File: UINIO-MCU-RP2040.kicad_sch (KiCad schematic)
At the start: 0 parts

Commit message: Part of the schematic diagram is drawn.
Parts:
- added C1, C2: 1uF, Capacitor_SMD:C_0603_1608Metric, symbol Device:C
- added C10, C13, C4, C5, C8, C9: 0.1uF, Capacitor_SMD:C_0603_1608Metric, symbol Device:C
- added C11, C3: 2.2uF, Capacitor_SMD:C_0603_1608Metric, symbol Device:C
- added C12: 1nF, Capacitor_SMD:C_0603_1608Metric, symbol Device:C
- added C6, C7: 12pF, Capacitor_SMD:C_0603_1608Metric, symbol Device:C
- added D1: LED_Red, LED_SMD:LED_0603_1608Metric, symbol Device:LED
- added D2: 1N5819, Diode_SMD:D_SOD-323F, symbol Diode:1N5819
- added J1: Conn_01x04_Pin, Connector_PinHeader_2.54mm:PinHeader_1x04_P2.54mm_Vertical, symbol Connector:Conn_01x04_Pin
- added J2, J3: Conn_01x20_Pin, symbol Connector:Conn_01x20_Pin
- added Q1: DMG1012T, Package_TO_SOT_SMD:SOT-523, symbol Transistor_FET:DMG1012T
- added R1, R2: 5.1K, Resistor_SMD:R_0603_1608Metric, symbol Device:R
- added R10: 1K, Resistor_SMD:R_0603_1608Metric, symbol Device:R
- added R11: 1.5K, Resistor_SMD:R_0603_1608Metric, symbol Device:R
- added R3: 2K, Resistor_SMD:R_0603_1608Metric, symbol Device:R
- added R4, R5: 27K, Resistor_SMD:R_0603_1608Metric, symbol Device:R
- added R6: 200R, Resistor_SMD:R_0603_1608Metric, symbol Device:R
- added R7: 1R, Resistor_SMD:R_0603_1608Metric, symbol Device:R
- added R8: 200K, Resistor_SMD:R_0603_1608Metric, symbol Device:R
- added R9: 100K, Resistor_SMD:R_0603_1608Metric, symbol Device:R
- added SW1: ~{USB_BOOT}, Uinio:KEY-SMD_4P-L4.2-W3.4-P2.15-LS4.7, symbol Uinio:Key_YTS_A016S_1
- added U1: RP2040, Package_DFN_QFN:QFN-56-1EP_7x7mm_P0.4mm_EP3.2x3.2mm, symbol MCU_RaspberryPi:RP2040
- added U2: ME6211C33M5G-N, Uinio:SOT-23-5_L3.0-W1.7-P0.95-LS2.8-BR, symbol Uinio:ME6211
- added U3: SPI-25-Flash-WSON8, Package_SON:WSON-8-1EP_6x5mm_P1.27mm_EP3.4x4.3mm, symbol Memory_Flash:W25Q32JVZP
- added USB1: USB_Type_C_16Pin, Uinio:USB-C-SMD_TYPEC-304J-BCP16, symbol Uinio:USB_Type_C_16Pin
- added Y1: 12MHz, Crystal:Crystal_SMD_3225-4Pin_3.2x2.5mm, symbol Device:Crystal_GND24
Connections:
- new net: C12.2, Q1.3 (D), R8.1, R9.2
- new net: R5.1, U1.46 (USB_DM)
- new net: R10.2, SW1.1, SW1.2
- new net: U1.20 (XIN), Y1.3
- new net: U1.21 (XOUT), Y1.1
- new net: R4.1, U1.47 (USB_DP)
- new net: C1.2, D2.1 (K), U2.1 (Vin), U2.3 (CE)
- new net: C7.2, Y1.2
- new net: R2.1, USB1.B5 (CC2)
- new net: D1.2 (A), R3.1
- new net: R1.1, USB1.A5 (CC1)
- new net: C6.2, Y1.4
- new net ADC_AVDD: C11.1, R7.2, U1.43 (ADC_AVDD)
- new net ADC_VREF: J2.6 (Pin_6), R6.2, R7.1
- new net Core_1.1V: C3.1, C4.1, C5.1, U1.23 (DVDD), U1.45 (VREG_VOUT), U1.50 (DVDD)
- new net GND: C1.1, C10.2, C11.2, C12.1, C13.2, C2.1, C3.2, C4.2, C5.2, C6.1, C7.1, C8.2, C9.2, D1.1 (K), J1.1 (Pin_1), J3.13 (Pin_13), J3.18 (Pin_18), J3.3 (Pin_3), J3.8 (Pin_8), R1.2, R2.2, R9.1, SW1.3, SW1.4, U1.19 (TESTEN), U1.57 (GND), U2.2 (Vss), U3.4 (GND), U3.9 (EP), USB1.13 (GND), USB1.14 (GND), USB1.15 (GND), USB1.16 (GND), USB1.A1B12 (GND), USB1.B1A12 (GND)
- new net GPIO0: J3.1 (Pin_1), U1.2 (GPIO0)
- new net GPIO1: J3.2 (Pin_2), U1.3 (GPIO1)
- new net GPIO10: J3.14 (Pin_14), U1.13 (GPIO10)
- new net GPIO11: J3.15 (Pin_15), U1.14 (GPIO11)
- new net GPIO12: J3.16 (Pin_16), U1.15 (GPIO12)
- new net GPIO13: J3.17 (Pin_17), U1.16 (GPIO13)
- new net GPIO14: J3.19 (Pin_19), U1.17 (GPIO14)
- new net GPIO15: J3.20 (Pin_20), U1.18 (GPIO15)
- new net GPIO16: J2.20 (Pin_20), U1.27 (GPIO16)
- new net GPIO17: J2.19 (Pin_19), U1.28 (GPIO17)
- new net GPIO18: J2.17 (Pin_17), U1.29 (GPIO18)
- new net GPIO19: J2.16 (Pin_16), U1.30 (GPIO19)
- new net GPIO2: J3.4 (Pin_4), U1.4 (GPIO2)
- new net GPIO20: J2.15 (Pin_15), U1.31 (GPIO20)
- new net GPIO21: J2.14 (Pin_14), U1.32 (GPIO21)
- new net GPIO22: J2.12 (Pin_12), U1.34 (GPIO22)
- new net GPIO23: U1.35 (GPIO23)
- new net GPIO24: U1.36 (GPIO24)
- new net GPIO25: U1.37 (GPIO25)
- new net GPIO26_ADC0: J2.10 (Pin_10), U1.38 (GPIO26_ADC0)
- new net GPIO27_ADC1: J2.9 (Pin_9), U1.39 (GPIO27_ADC1)
- new net GPIO28_ADC2: J2.7 (Pin_7), U1.40 (GPIO28_ADC2)
- new net GPIO29_ADC3: Q1.2 (S), U1.41 (GPIO29_ADC3)
- new net GPIO3: J3.5 (Pin_5), U1.5 (GPIO3)
- new net GPIO4: J3.6 (Pin_6), U1.6 (GPIO4)
- new net GPIO5: J3.7 (Pin_7), U1.7 (GPIO5)
- new net GPIO6: J3.9 (Pin_9), U1.8 (GPIO6)
- new net GPIO7: J3.10 (Pin_10), U1.9 (GPIO7)
- new net GPIO8: J3.11 (Pin_11), U1.11 (GPIO8)
- new net GPIO9: J3.12 (Pin_12), U1.12 (GPIO9)
- new net QSPI_SCLK: U1.52 (QSPI_SCLK), U3.6 (CLK)
- new net QSPI_SD0: U1.53 (QSPI_SD0), U3.5 (DI(IO0))
- new net QSPI_SD1: U1.55 (QSPI_SD1), U3.2 (DO(IO1))
- new net QSPI_SD2: U1.54 (QSPI_SD2), U3.3 (IO2)
- new net QSPI_SD3: U1.51 (QSPI_SD3), U3.7 (IO3)
- new net QSPI_SS: R10.1, R11.2, U1.56 (QSPI_SS), U3.1 (~{CS})
- new net RUN: J2.11 (Pin_11), U1.26 (RUN)
- new net SWCLK: J1.2 (Pin_2), U1.24 (SWCLK)
- new net SWD: J1.3 (Pin_3), U1.25 (SWD)
- new net USB_Data+: R4.2, USB1.A6 (DP1), USB1.B6 (DP2)
- new net USB_Data-: R5.2, USB1.A7 (DN1), USB1.B7 (DN2)
- new net VDD_3.3V: C10.1, C13.1, C2.2, C8.1, C9.1, J1.4 (Pin_4), J2.5 (Pin_5), Q1.1 (G), R11.1, R3.2, R6.1, U1.1 (IOVDD), U1.10 (IOVDD), U1.22 (IOVDD), U1.33 (IOVDD), U1.42 (IOVDD), U1.44 (VREG_IN), U1.48 (USB_VDD), U1.49 (IOVDD), U2.5 (Vout), U3.8 (VCC)
- new net VDD_5V: D2.2 (A), J2.1 (Pin_1), R8.2, USB1.A4B9 (VBUS), USB1.B4A9 (VBUS)
- no-connect marks 0 -> 3
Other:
- note added: "3.3V 线性稳压电路"
- note added: "USB Type-C 接口电路"

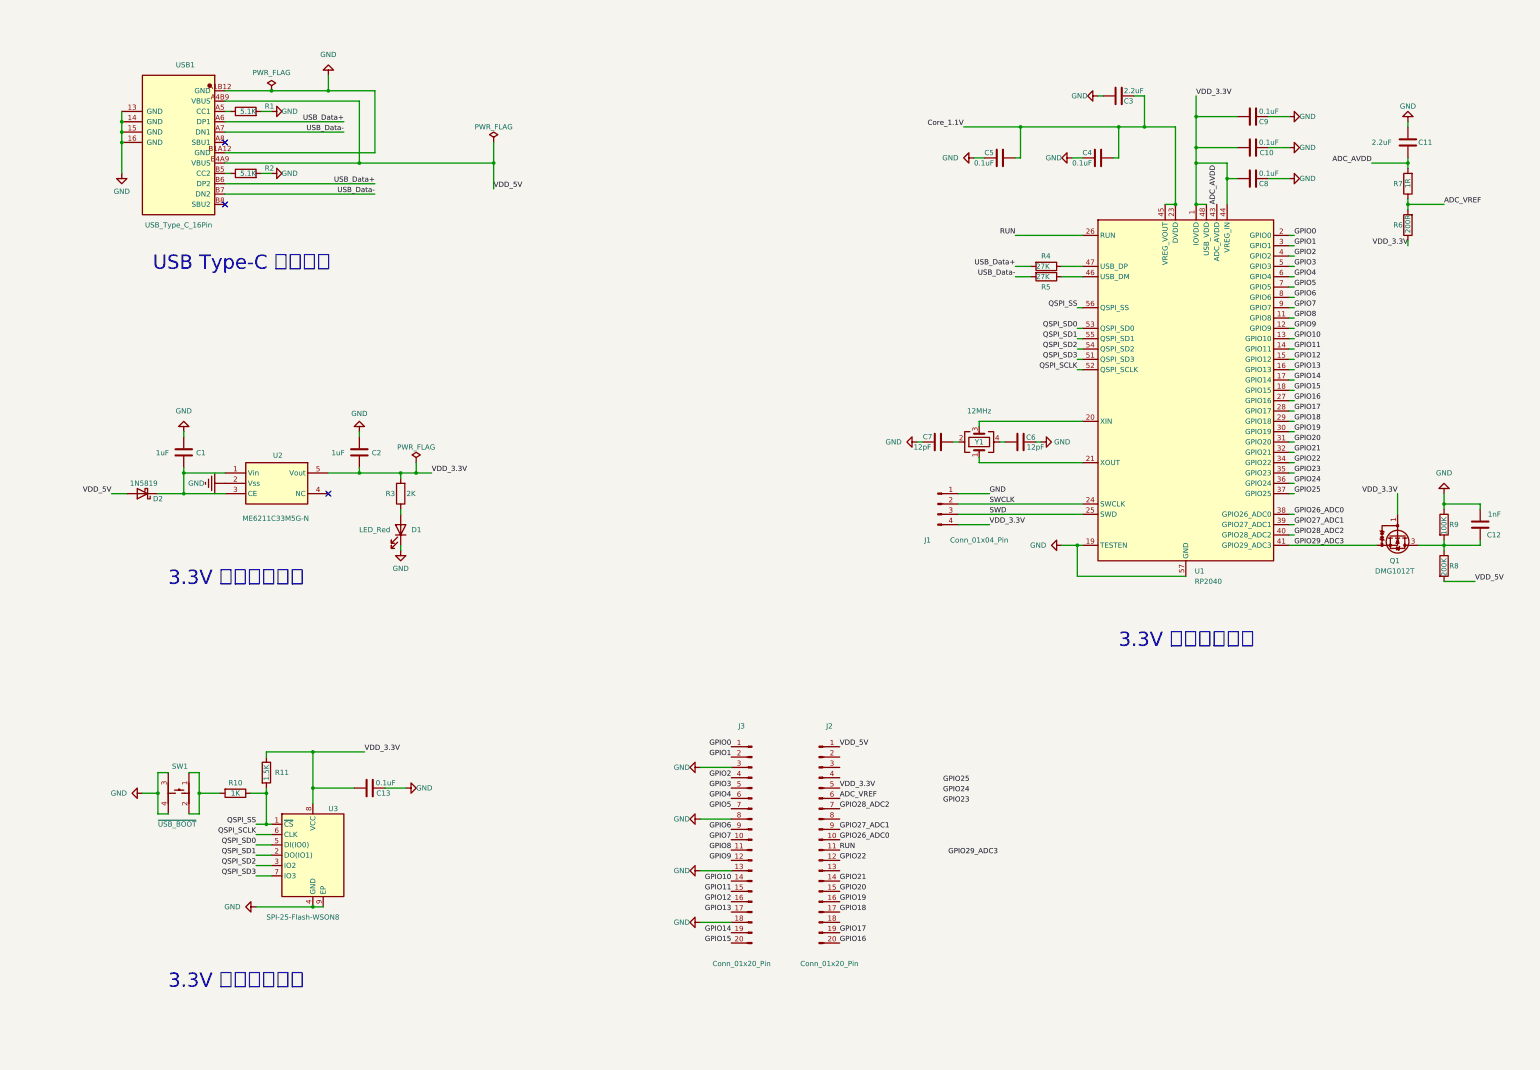
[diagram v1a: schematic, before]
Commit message: Complete the schematic drawing.
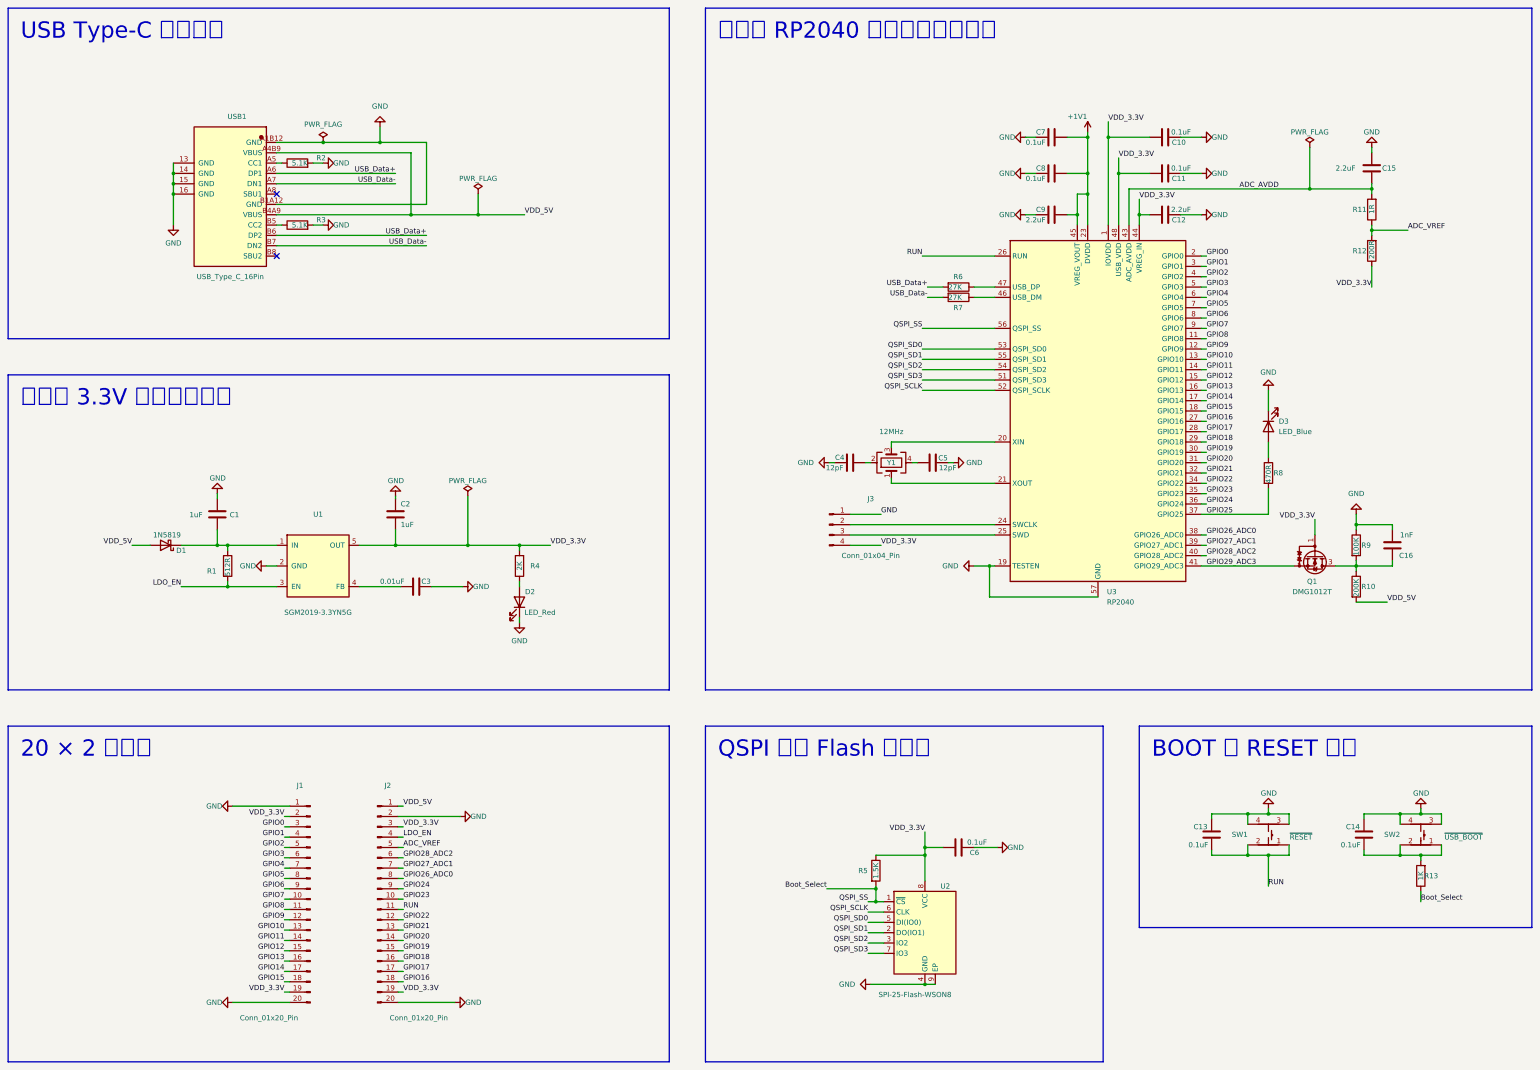
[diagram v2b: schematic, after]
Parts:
- removed D1: LED_Red, LED_SMD:LED_0603_1608Metric, symbol Device:LED
- removed D2: 1N5819, Diode_SMD:D_SOD-323F, symbol Diode:1N5819
- removed J1: Conn_01x04_Pin, Connector_PinHeader_2.54mm:PinHeader_1x04_P2.54mm_Vertical, symbol Connector:Conn_01x04_Pin
- removed R3: 2K, Resistor_SMD:R_0603_1608Metric, symbol Device:R
- removed U2: ME6211C33M5G-N, Uinio:SOT-23-5_L3.0-W1.7-P0.95-LS2.8-BR, symbol Uinio:ME6211
- added C13, C14: 0.1uF, Capacitor_SMD:C_0603_1608Metric, symbol Device:C
- added C3: 0.01uF, Capacitor_SMD:C_0603_1608Metric, symbol Device:C
- added D1: 1N5819, Diode_SMD:D_SOD-323F, symbol Diode:1N5819
- added D2: LED_Red, LED_SMD:LED_0603_1608Metric, symbol Device:LED
- added D3: LED_Blue, LED_SMD:LED_0603_1608Metric, symbol Device:LED
- added J3: Conn_01x04_Pin, Connector_PinHeader_2.54mm:PinHeader_1x04_P2.54mm_Vertical, symbol Connector:Conn_01x04_Pin
- added R1: 512R, Resistor_SMD:R_0603_1608Metric, symbol Device:R
- added R4: 2K, Resistor_SMD:R_0603_1608Metric, symbol Device:R
- added R8: 470R, Resistor_SMD:R_0603_1608Metric, symbol Device:R
- added SW1: ~{RESET}, Uinio:KEY-SMD_4P-L4.2-W3.4-P2.15-LS4.7, symbol Uinio:Key_YTS_A016S_1
- added U1: SGM2019-3.3YN5G, Uinio:SOT-23-5_L3.0-W1.7-P0.95-LS2.8-BR, symbol Uinio:SGM2019-3.3YN5G
- C12: renamed from C8; value 0.1uF -> 2.2uF
- J1: renamed from J3; footprint (none) -> Connector_PinHeader_2.54mm:PinHeader_1x20_P2.54mm_Vertical
- J2: footprint (none) -> Connector_PinHeader_2.54mm:PinHeader_1x20_P2.54mm_Vertical
- renumbered C9 to C10, C10 to C11, C11 to C15, C12 to C16, C7 to C4, C6 to C5, C13 to C6, C5 to C7, C4 to C8, C3 to C9, R8 to R10, R7 to R11, R6 to R12, R10 to R13, R1 to R2, R2 to R3, R11 to R5, R4 to R6, R5 to R7, SW1 to SW2, U3 to U2, U1 to U3
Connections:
- net ADC_VREF: now also J2.5 (Pin_5); no longer J2.6 (Pin_6)
- net GND: now also J1.1 (Pin_1), J1.20 (Pin_20), J2.2 (Pin_2), J2.20 (Pin_20), C13.2, C14.2, C3.1, D2.1 (K), D3.1 (K), J3.1 (Pin_1), SW1.3, SW1.4, U1.2 (GND); no longer J1.13 (Pin_13), J1.18 (Pin_18), J1.3 (Pin_3), J1.8 (Pin_8)
- net GPIO0: now also J1.3 (Pin_3); no longer J1.1 (Pin_1)
- net GPIO1: now also J1.4 (Pin_4); no longer J1.2 (Pin_2)
- net GPIO10: now also J1.13 (Pin_13); no longer J1.14 (Pin_14)
- net GPIO11: now also J1.14 (Pin_14); no longer J1.15 (Pin_15)
- net GPIO12: now also J1.15 (Pin_15); no longer J1.16 (Pin_16)
- net GPIO13: now also J1.16 (Pin_16); no longer J1.17 (Pin_17)
- net GPIO14: now also J1.17 (Pin_17); no longer J1.19 (Pin_19)
- net GPIO15: now also J1.18 (Pin_18); no longer J1.20 (Pin_20)
- net GPIO16: now also J2.18 (Pin_18); no longer J2.20 (Pin_20)
- net GPIO17: now also J2.17 (Pin_17); no longer J2.19 (Pin_19)
- net GPIO18: now also J2.16 (Pin_16); no longer J2.17 (Pin_17)
- net GPIO19: now also J2.15 (Pin_15); no longer J2.16 (Pin_16)
- net GPIO2: now also J1.5 (Pin_5); no longer J1.4 (Pin_4)
- net GPIO20: now also J2.14 (Pin_14); no longer J2.15 (Pin_15)
- net GPIO21: now also J2.13 (Pin_13); no longer J2.14 (Pin_14)
- net GPIO23: now also J2.10 (Pin_10)
- net GPIO24: now also J2.9 (Pin_9)
- net GPIO25: now also R8.2
- net GPIO26_ADC0: now also J2.8 (Pin_8); no longer J2.10 (Pin_10)
- net GPIO27_ADC1: now also J2.7 (Pin_7); no longer J2.9 (Pin_9)
- net GPIO28_ADC2: now also J2.6 (Pin_6); no longer J2.7 (Pin_7)
- net GPIO3: now also J1.6 (Pin_6); no longer J1.5 (Pin_5)
- net GPIO4: now also J1.7 (Pin_7); no longer J1.6 (Pin_6)
- net GPIO5: now also J1.8 (Pin_8); no longer J1.7 (Pin_7)
- net RUN: now also C13.1, SW1.1, SW1.2
- net VDD_3.3V: now also J1.19 (Pin_19), J1.2 (Pin_2), J2.19 (Pin_19), J2.3 (Pin_3), J3.4 (Pin_4), R4.2, U1.5 (OUT); no longer J2.5 (Pin_5)
- net VDD_5V: now also D1.2 (A)
- net at R13.2, SW2.1, SW2.2: now also C14.1
- net LDO_EN: now reaches J2.4 (Pin_4)
- net LDO_EN: now also R1.2, U1.3 (EN)
- net at C1.2: now also D1.1 (K), R1.1, U1.1 (IN)
- net Core_1.1V renamed +1V1
- net QSPI_SS renamed Boot_Select
- net SWCLK: no longer names the net of U3.24 (SWCLK)
- net SWCLK: now also J3.2 (Pin_2)
- net SWD: no longer names the net of U3.25 (SWD)
- net SWD: now also J3.3 (Pin_3)
- new net: D2.2 (A), R4.1
- new net: C3.2, U1.4 (FB)
- new net: D3.2 (A), R8.1
- no-connect marks 3 -> 2
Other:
- note removed: "3.3V 线性稳压电路"
- note removed: "USB Type-C 接口电路"
- moved on the sheet: C10, C11, C12, C15, C16, C4, C5, C6, C7, C8, C9, J1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

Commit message: Finish PCB layout.
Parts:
- C10, C11, C12, C13, C14, C15, C16, C4, C5, C6, C7, C8, C9: footprint Capacitor_SMD:C_0603_1608Metric -> Capacitor_SMD:C_0402_1005Metric
- R10, R11, R13, R5, R6, R7, R8, R9: footprint Resistor_SMD:R_0603_1608Metric -> Resistor_SMD:R_0402_1005Metric
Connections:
- net USB_Data+: now also R6.1, U3.47 (USB_DP); no longer R6.2, USB1.A6 (DP1), USB1.B6 (DP2)
- net USB_Data-: now also R7.1, U3.46 (USB_DM); no longer R7.2, USB1.A7 (DN1), USB1.B7 (DN2)
- net VDD_5V: now also C1.2, D1.1 (K), R1.1, U1.1 (IN); no longer D1.2 (A), USB1.A4B9 (VBUS), USB1.B4A9 (VBUS)
- new net: R6.2, USB1.A6 (DP1), USB1.B6 (DP2)
- new net: R7.2, USB1.A7 (DN1), USB1.B7 (DN2)
- new net USB_5V: D1.2 (A), USB1.A4B9 (VBUS), USB1.B4A9 (VBUS)
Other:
- moved on the sheet: R4

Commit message: Complete PCB wiring.
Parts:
- added C17: 0.1uF, Capacitor_SMD:C_0402_1005Metric, symbol Device:C
- D1: footprint Diode_SMD:D_SOD-323F -> Diode_SMD:D_SOD-123
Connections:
- net GND: now also J2.1 (Pin_1), J2.3 (Pin_3), J3.4 (Pin_4), C17.2; no longer J2.2 (Pin_2), J3.1 (Pin_1)
- net GPIO16: now also J2.17 (Pin_17); no longer J2.18 (Pin_18)
- net GPIO17: now also J2.16 (Pin_16); no longer J2.17 (Pin_17)
- net GPIO18: now also J2.15 (Pin_15); no longer J2.16 (Pin_16)
- net GPIO19: now also J2.14 (Pin_14); no longer J2.15 (Pin_15)
- net GPIO20: now also J2.13 (Pin_13); no longer J2.14 (Pin_14)
- net GPIO21: now also J2.12 (Pin_12); no longer J2.13 (Pin_13)
- net GPIO22: now also J2.11 (Pin_11); no longer J2.12 (Pin_12)
- net RUN: now also J2.18 (Pin_18); no longer J2.11 (Pin_11)
- net VDD_3.3V: now also J2.2 (Pin_2), J3.1 (Pin_1), C17.1; no longer J1.2 (Pin_2), J2.3 (Pin_3), J3.4 (Pin_4)
- net VDD_5V: now also J1.2 (Pin_2); no longer J2.1 (Pin_1)
- net at J3.2 (Pin_2): now also U3.25 (SWD); no longer U3.24 (SWCLK)
- net at J3.3 (Pin_3): now also U3.24 (SWCLK); no longer U3.25 (SWD)
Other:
- moved on the sheet: C1, C12, C14, C6, D1, J1, J2, R1, R13, R6, R7, SW2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
